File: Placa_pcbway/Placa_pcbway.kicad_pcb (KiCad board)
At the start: 2 copper layers, 100 x 100 mm, 69 parts, among them J1 Screw_Terminal_Crusher1, J2 MixerScrewTerminal1, J3 FanScrewTerminal1, K1 FINDER-36.11, K2 FINDER-36.11, K3 FINDER-36.11, Q1 2N3904, Q2 2N3904, Q3 2N3904, U1 LM7805_TO220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

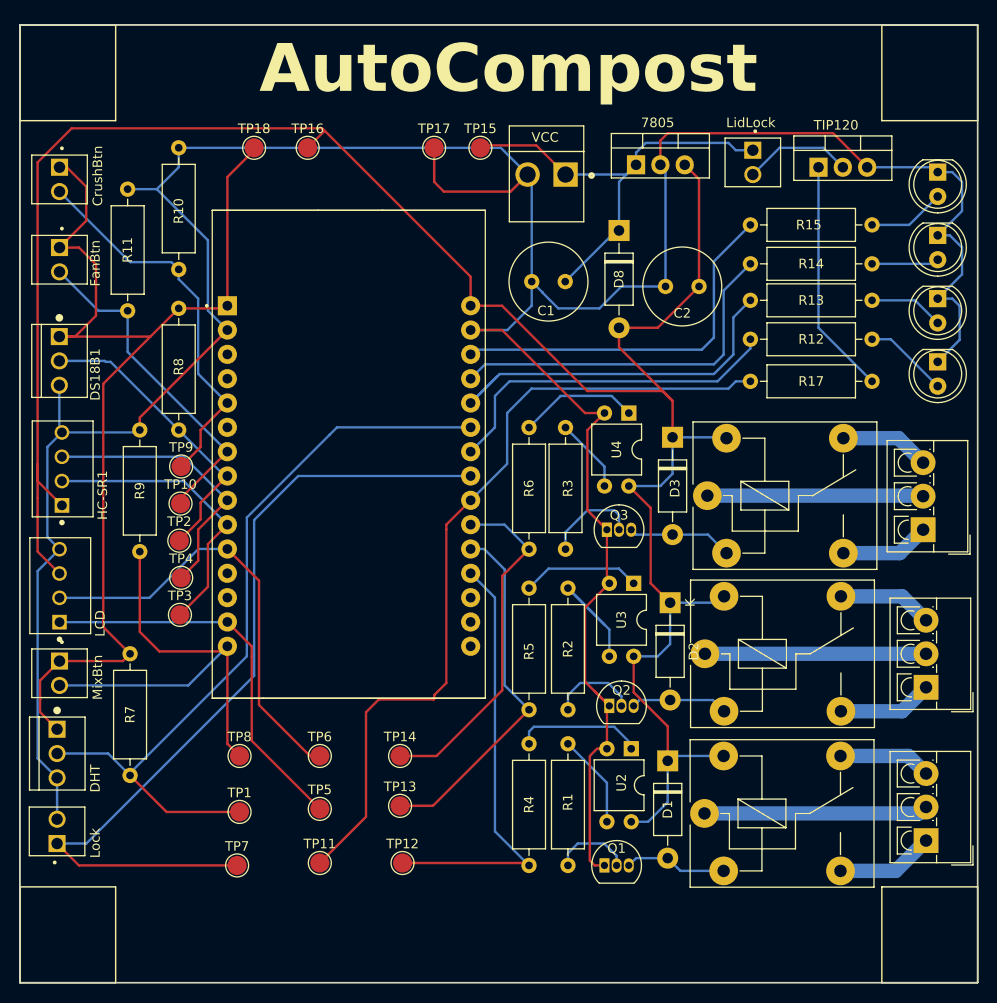
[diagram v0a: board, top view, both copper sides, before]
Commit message: Placa Pcbway terminada
Se agrandaron los agujeros correspondientes, se agregaron los agujeros de placa y el DRC pass
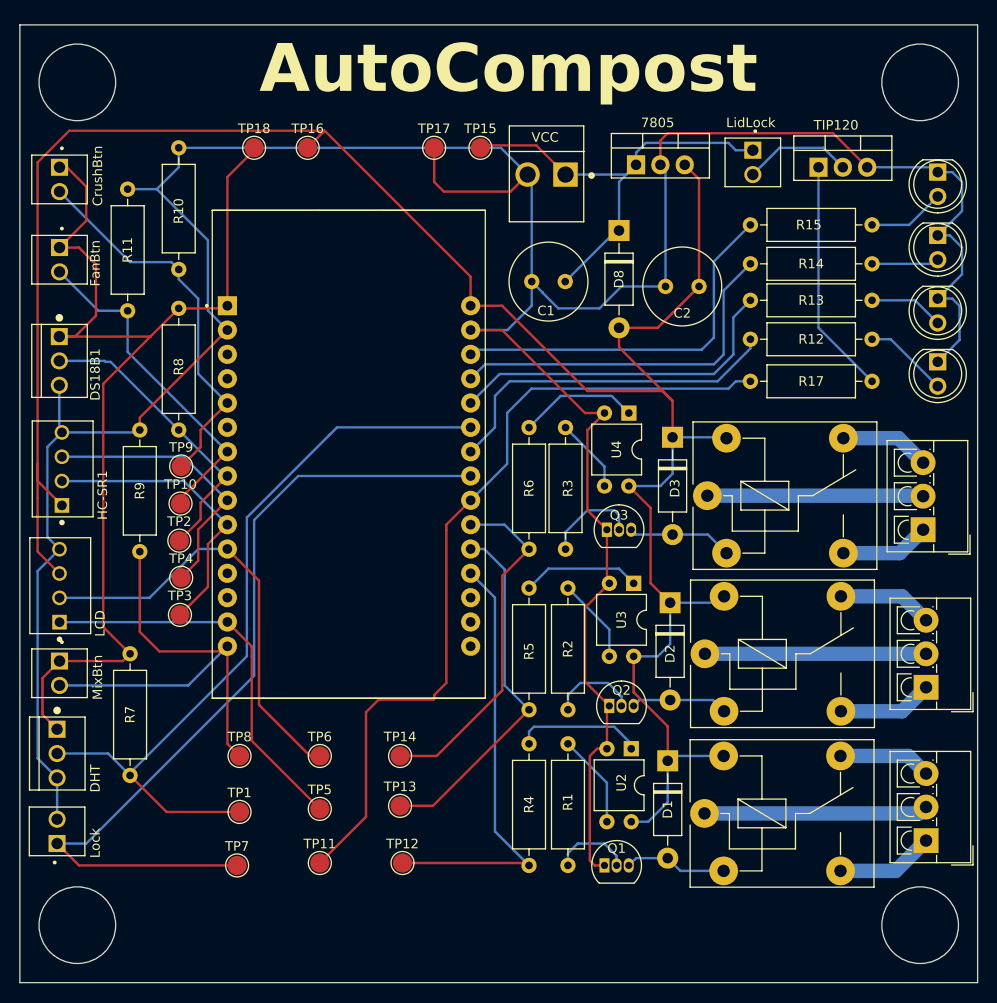
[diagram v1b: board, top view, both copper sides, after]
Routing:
- net Net-(R2-Pad1): track 14.3 -> 8.91 mm
- net /Led2: track 39.8 -> 35.9 mm
- net GND: track 334.6 -> 332.5 mm
- net /3V3: track 115.5 -> 115.0 mm
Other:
- outline, holes or cut-outs redrawn

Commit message: Placa pcbway terminada sin plano de tierra
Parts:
- removed D7: LED, LED_THT:LED_D5.0mm
- removed R15: 220, Resistor_THT:R_Axial_DIN0309_L9.0mm_D3.2mm_P12.70mm_Horizontal
- J1: value Screw_Terminal_Crusher1 -> Molex 0.156; footprint TerminalBlock_4Ucon:TerminalBlock_4Ucon_1x03_P3.50mm_Vertical -> Conectores_Molex:Molex_156_3pines
- J2: value MixerScrewTerminal1 -> Molex 0.156; footprint TerminalBlock_4Ucon:TerminalBlock_4Ucon_1x03_P3.50mm_Vertical -> Conectores_Molex:Molex_156_3pines
- J3: value FanScrewTerminal1 -> Molex 0.156; footprint TerminalBlock_4Ucon:TerminalBlock_4Ucon_1x03_P3.50mm_Vertical -> Conectores_Molex:Molex_156_3pines
- moved J2 3.53 mm to (195.1, 105.7), turned to -90 degrees
- moved J1 3.28 mm to (195.1, 121.9), turned to -90 degrees
- moved J3 3.14 mm to (195.1, 89.7), turned to -90 degrees
- moved K1 0.25 mm to (171.7, 122.3)
- moved K2 0.20 mm to (171.7, 105.7)
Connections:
- U5 pad 19: /Crusher -> /Lid
- U5 pad 20: /Mixer -> unconnected-(U5-D35-Pad20)
- U5 pad 22: /Lock -> /Crusher
- U5 pad 23: /Lid -> /Mixer
- U5 pad 24: /Led1 -> /Lock
- U5 pad 26: /Led2 -> /Led1
- U5 pad 27: /Led3 -> /Led2
- U5 pad 28: /Led4 -> /Led3
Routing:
- net /Led4: track 39.5 -> 0.00 mm
- net /Lid: track 88.3 -> 78.2 mm
- net Net-(D7-A): track 8.60 -> 0.00 mm
- net /Crusher: track 46.3 -> 54.0 mm
- net /Mixer: track 37.8 -> 44.5 mm
- net GND: track 332.5 -> 327.4 mm
- net /Led3: track 38.4 -> 33.8 mm
- net /Led1: track 36.6 -> 32.0 mm
- net /Led2: track 35.9 -> 33.4 mm
- net Net-(J3-Pad3): track 9.39 -> 10.1 mm
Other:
- outline, holes or cut-outs redrawn
- board text added: "CRUSHER"
- board text added: "FAN"
- board text added: "MIXER"

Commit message: Placa con plano de tierra
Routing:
- added copper zone on B.Cu, net GND
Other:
- outline, holes or cut-outs redrawn
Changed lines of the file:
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@@
   (gr_circle (center 106 46) (end 110 46)
+    (stroke (width 0.1) (type default)) (fill none) (layer "Edge.Cuts"))
+  (gr_rect (start 184.15 80.137) (end 197.866 80.899)
     (stroke (width 0.1) (type default)) (fill none) (layer "Edge.Cuts"))
   (gr_text "DS18B1" (at 108.458 79.248 90) (layer "F.SilkS")
@@
   (segment (start 194.302 85.702) (end 195.072 85.702) (width 1.5) (layer "B.Cu") (net 56))
   (segment (start 191.754 83.154) (end 194.302 85.702) (width 1.5) (layer "B.Cu") (net 56))
+  (zone (net 2) (net_name "GND") (layer "B.Cu") (hatch edge 0.5)
+    (connect_pads (clearance 0.5))
+    (min_thickness 0.25) (filled_areas_thickness no)
+    (fill yes (thermal_gap 0.5) (thermal_bridge_width 0.5))
+    (polygon
+      (pts
+        (xy 170.053 79.756)
+        (xy 199.517 79.756)
+        (xy 199.517 50.546)
+        (xy 100.965 50.419)
+        (xy 100.838 128.778)
+        (xy 169.926 128.905)
+        (xy 169.926 125.222)
+        (xy 168.402 123.698)
+        (xy 168.402 121.158)
+        (xy 169.926 119.507)
+        (xy 169.926 108.204)
+        (xy 168.656 107.061)
+        (xy 168.656 104.394)
+        (xy 169.926 102.997)
+        (xy 169.926 91.948)
+        (xy 168.656 90.678)
+        (xy 168.656 87.884)
+        (xy 170.053 86.233)
+      )
+    )
+  )
 )

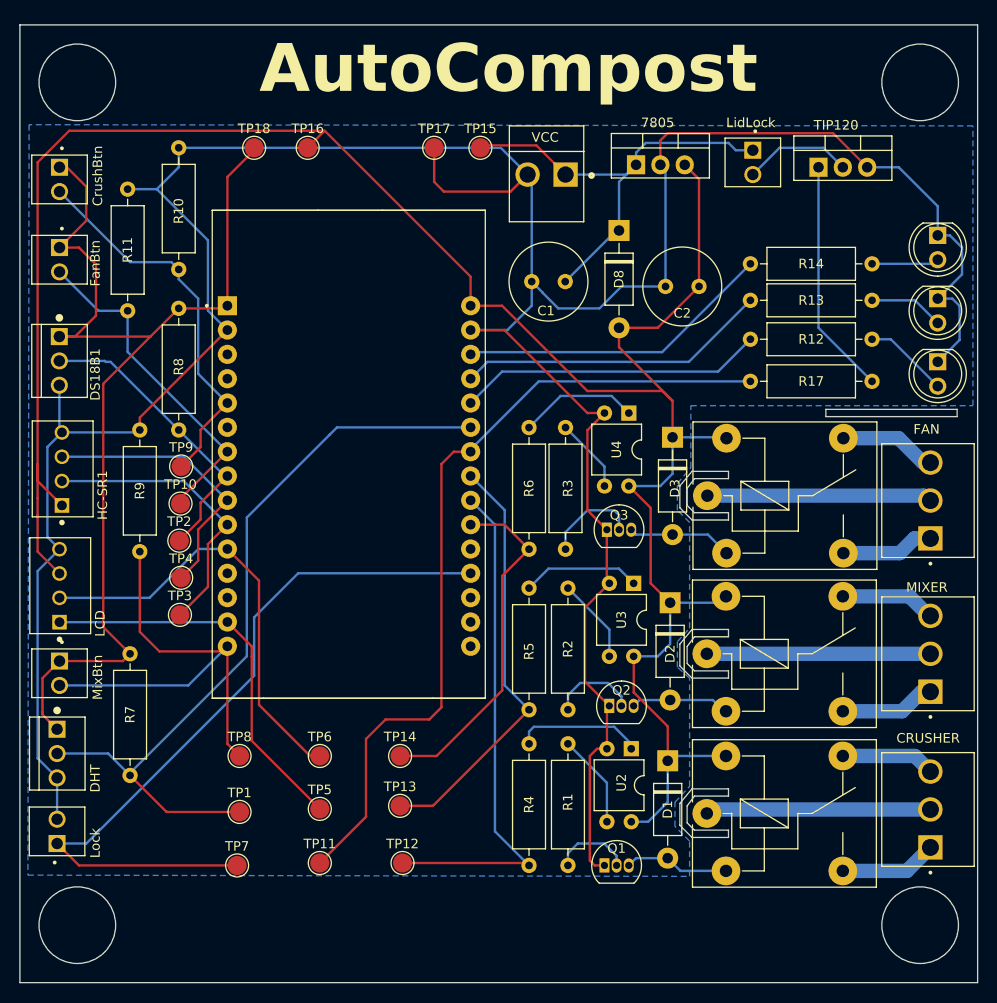
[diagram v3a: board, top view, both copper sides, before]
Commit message: Correccion Fan Button
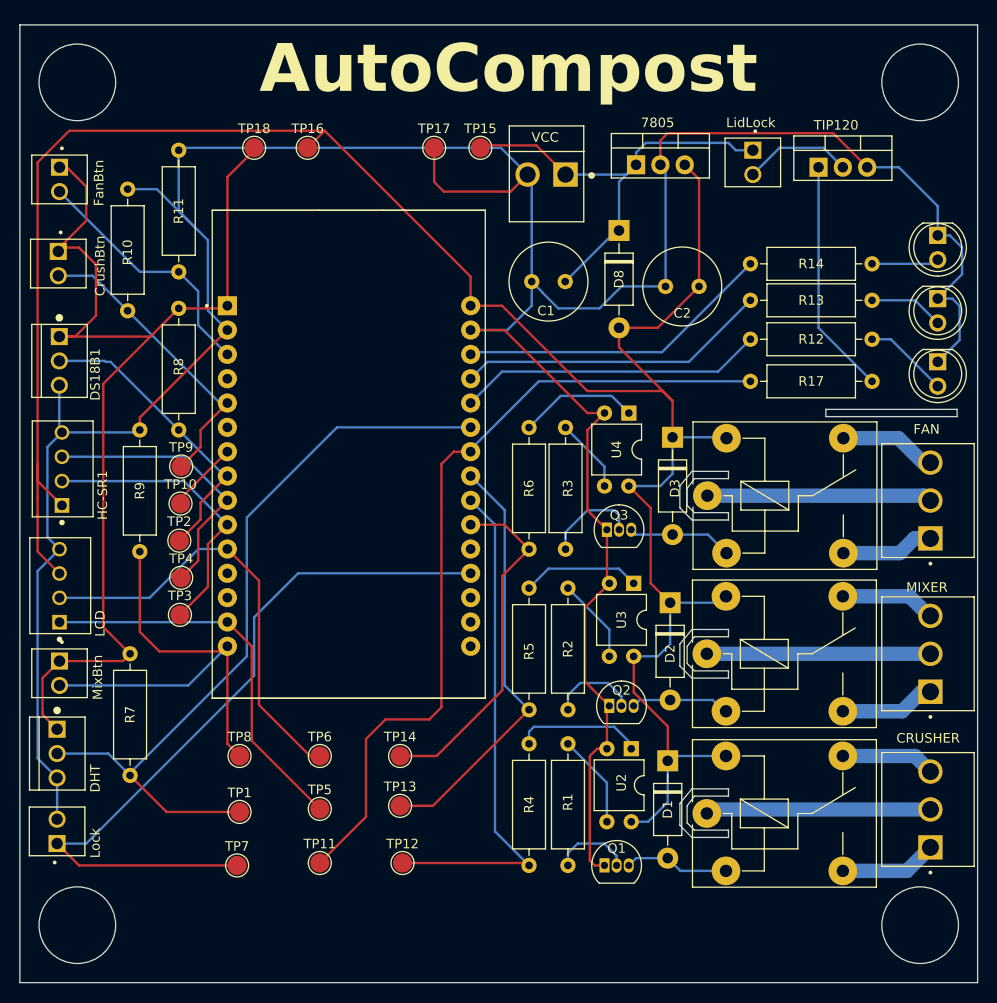
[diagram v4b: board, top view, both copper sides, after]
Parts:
- moved CrusherButton1 8.78 mm to (104.0, 64.9)
- moved FanButton1 8.38 mm to (104.1, 56.1)
- moved R10 6.86 mm to (111.3, 57.1)
- moved R11 6.71 mm to (116.6, 53.1)
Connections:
- U5 pad 3: unconnected-(U5-D15-Pad3) -> /FanBtn
- U5 pad 7: /FanBtn -> unconnected-(U5-TX2-Pad7)
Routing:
- net /CrusherBtn: track 40.5 -> 31.8 mm
- net GND: track 327.4 -> 332.8 mm
- net /FanBtn: track 35.3 -> 34.1 mm
- removed copper zone on B.Cu, net GND
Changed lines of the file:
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@@
   (net 44 "unconnected-(U5-VP-Pad17)")
   (net 45 "unconnected-(U5-EN-Pad16)")
-  (net 46 "unconnected-(U5-D15-Pad3)")
+  (net 46 "unconnected-(U5-TX2-Pad7)")
   (net 47 "unconnected-(U5-D35-Pad20)")
   (net 48 "Net-(J1-Pad1)")
@@
   )
   (footprint "Resistor_THT:R_Axial_DIN0309_L9.0mm_D3.2mm_P12.70mm_Horizontal" (layer "F.Cu")
-    (at 116.586 52.832 -90)
+    (at 111.252 57.15 -90)
     (descr "Resistor, Axial_DIN0309 series, Axial, Horizontal, pin pitch=12.7mm, 0.5W = 1/2W, length*diameter=9*3.2mm^2, http://cdn-reichelt.de/documents/datenblatt/B400/1_4W%23YAG.pdf")
     (tags "Resistor Axial_DIN0309 series Axial Horizontal pin pitch 12.7mm 0.5W = 1/2W length 9mm diameter 3.2mm")
@@
   )
   (footprint "Resistor_THT:R_Axial_DIN0309_L9.0mm_D3.2mm_P12.70mm_Horizontal" (layer "F.Cu")
-    (at 111.252 57.15 -90)
+    (at 116.586 53.086 -90)
     (descr "Resistor, Axial_DIN0309 series, Axial, Horizontal, pin pitch=12.7mm, 0.5W = 1/2W, length*diameter=9*3.2mm^2, http://cdn-reichelt.de/documents/datenblatt/B400/1_4W%23YAG.pdf")
     (tags "Resistor Axial_DIN0309 series Axial Horizontal pin pitch 12.7mm 0.5W = 1/2W length 9mm diameter 3.2mm")
@@
         (effects (font (size 1 1) (thickness 0.15)))
     )
-    (fp_text value "TestPoint" (at 0 2.05) (layer "F.Fab")
+    (fp_text value "TestPoint" (at 0 2.05) (layer "F.Fab") hide
         (effects (font (size 1 1) (thickness 0.15)))
     )
@@
         (effects (font (size 1 1) (thickness 0.15)))
     )
-    (fp_text value "TestPoint" (at 0 2.05) (layer "F.Fab")
+    (fp_text value "TestPoint" (at 0 2.05) (layer "F.Fab") hide
         (effects (font (size 1 1) (thickness 0.15)))
     )
@@
   )
   (footprint "Conectores_Molex:Molex_100_2pines" (layer "F.Cu")
-    (at 104.14 56.134 90)
+    (at 104.013 64.918 90)
     (property "Availability" "In Stock")
     (property "Check_prices" "https://www.snapeda.com/parts/0022272021/Molex/view-part/?ref=eda")
@@
       (net 2 "GND") (pinfunction "GND") (pintype "power_in") (solder_mask_margin 0.102))
     (pad "3" thru_hole circle (at -12.7 -10.435) (size 2 2) (drill 1.02) (layers "*.Cu" "*.Mask")
-      (net 46 "unconnected-(U5-D15-Pad3)") (pinfunction "D15") (pintype "bidirectional") (solder_mask_margin 0.102))
+      (net 14 "/FanBtn") (pinfunction "D15") (pintype "bidirectional") (solder_mask_margin 0.102))
     (pad "4" thru_hole circle (at -12.7 -7.895) (size 2 2) (drill 1.02) (layers "*.Cu" "*.Mask")
       (net 42 "unconnected-(U5-D2-Pad4)") (pinfunction "D2") (pintype "bidirectional") (solder_mask_margin 0.102))
@@
       (net 39 "unconnected-(U5-RX2-Pad6)") (pinfunction "RX2") (pintype "input") (solder_mask_margin 0.102))
     (pad "7" thru_hole circle (at -12.7 -0.275) (size 2 2) (drill 1.02) (layers "*.Cu" "*.Mask")
-      (net 14 "/FanBtn") (pinfunction "TX2") (pintype "output") (solder_mask_margin 0.102))
+      (net 46 "unconnected-(U5-TX2-Pad7)") (pinfunction "TX2") (pintype "output") (solder_mask_margin 0.102))
     (pad "8" thru_hole circle (at -12.7 2.265) (size 2 2) (drill 1.02) (layers "*.Cu" "*.Mask")
       (net 13 "/DS18B20") (pinfunction "D5") (pintype "bidirectional") (solder_mask_margin 0.102))
@@
   )
   (footprint "Conectores_Molex:Molex_100_2pines" (layer "F.Cu")
-    (at 104.14 64.516 90)
+    (at 104.14 56.134 90)
     (property "Availability" "In Stock")
     (property "Check_prices" "https://www.snapeda.com/parts/0022272021/Molex/view-part/?ref=eda")
@@
     (effects (font (size 1 1) (thickness 0.15)) (justify left bottom))
   )
-  (gr_text "CrushBtn" (at 108.712 58.928 90) (layer "F.SilkS")
+  (gr_text "CrushBtn" (at 108.966 68.326 90) (layer "F.SilkS")
     (effects (font (size 1 1) (thickness 0.15)) (justify left bottom))
   )
@@
     (effects (font (size 1 1) (thickness 0.15)) (justify left bottom))
   )
-  (gr_text "FanBtn" (at 108.458 67.31 90) (layer "F.SilkS")
+  (gr_text "FanBtn" (at 108.839 58.928 90) (layer "F.SilkS")
     (effects (font (size 1 1) (thickness 0.15)) (justify left bottom))
   )
@@
   (segment (start 161.29 98.049) (end 161.549 98.308) (width 0.25) (layer "F.Cu") (net 2))
   (segment (start 195.834 68.58) (end 197.358 68.58) (width 0.25) (layer "B.Cu") (net 2))
-  (segment (start 114.3 57.15) (end 116.586 54.864) (width 0.25) (layer "B.Cu") (net 2))
   (segment (start 167.414 55.146) (end 166.878 54.61) (width 0.25) (layer "B.Cu") (net 2))
   (segment (start 195.834 61.976) (end 197.104 61.976) (width 0.25) (layer "B.Cu") (net 2))
-  (segment (start 114.3 57.15) (end 119.634 62.484) (width 0.25) (layer "B.Cu") (net 2))
   (segment (start 104.12 82.276) (end 104.394 82.55) (width 0.25) (layer "B.Cu") (net 2))
   (segment (start 153.444 66.802) (end 154.587 67.945) (width 0.25) (layer "B.Cu") (net 2))
@@
   (segment (start 103.886 122.936) (end 103.886 118.618) (width 0.25) (layer "B.Cu") (net 2))
   (segment (start 197.358 68.58) (end 198.12 69.342) (width 0.25) (layer "B.Cu") (net 2))
+  (segment (start 116.586 53.086) (end 116.586 59.436) (width 0.25) (layer "B.Cu") (net 2))
   (segment (start 104.12 77.6235) (end 104.12 82.276) (width 0.25) (layer "B.Cu") (net 2))
   (segment (start 111.252 57.15) (end 114.3 57.15) (width 0.25) (layer "B.Cu") (net 2))
@@
   (segment (start 102.87 93.472) (end 104.14 94.742) (width 0.25) (layer "B.Cu") (net 2))
   (segment (start 198.374 63.246) (end 198.374 66.04) (width 0.25) (layer "B.Cu") (net 2))
+  (segment (start 116.586 59.436) (end 118.237 61.087) (width 0.25) (layer "B.Cu") (net 2))
+  (segment (start 118.237 61.087) (end 119.634 62.484) (width 0.25) (layer "B.Cu") (net 2))
   (segment (start 198.374 66.04) (end 195.834 68.58) (width 0.25) (layer "B.Cu") (net 2))
   (segment (start 153.444 69.314) (end 153.444 66.802) (width 0.25) (layer "B.Cu") (net 2))
+  (segment (start 114.3 57.15) (end 118.237 61.087) (width 0.25) (layer "B.Cu") (net 2))
   (segment (start 198.12 69.342) (end 198.12 72.893) (width 0.25) (layer "B.Cu") (net 2))
   (segment (start 147.066 71.861) (end 150.897 71.861) (width 0.25) (layer "B.Cu") (net 2))
@@
   (segment (start 118.872 82.296) (end 121.666 79.502) (width 0.25) (layer "F.Cu") (net 5))
   (segment (start 116.84 86.106) (end 118.872 84.074) (width 0.25) (layer "F.Cu") (net 5))
-  (segment (start 111.506 64.77) (end 115.824 64.77) (width 0.25) (layer "B.Cu") (net 5))
-  (segment (start 104.14 57.404) (end 111.506 64.77) (width 0.25) (layer "B.Cu") (net 5))
-  (segment (start 118.618 76.433) (end 121.666 79.481) (width 0.25) (layer "B.Cu") (net 5))
-  (segment (start 115.824 64.77) (end 116.586 65.532) (width 0.25) (layer "B.Cu") (net 5))
-  (segment (start 118.618 68.58) (end 118.618 76.433) (width 0.25) (layer "B.Cu") (net 5))
-  (segment (start 116.586 65.532) (end 116.586 66.548) (width 0.25) (layer "B.Cu") (net 5))
-  (segment (start 116.586 66.548) (end 118.618 68.58) (width 0.25) (layer "B.Cu") (net 5))
+  (segment (start 111.252 69.85) (end 120.883 79.481) (width 0.25) (layer "B.Cu") (net 5))
+  (segment (start 120.883 79.481) (end 121.666 79.481) (width 0.25) (layer "B.Cu") (net 5))
+  (segment (start 104.013 66.188) (end 107.59 66.188) (width 0.25) (layer "B.Cu") (net 5))
+  (segment (start 107.59 66.188) (end 111.252 69.85) (width 0.25) (layer "B.Cu") (net 5))
   (segment (start 167.64 127) (end 164.338 127) (width 0.25) (layer "B.Cu") (net 6))
   (segment (start 164.338 127) (end 163.576 127.762) (width 0.25) (layer "B.Cu") (net 6))
@@
   (segment (start 116.7765 89.4505) (end 116.7765 89.9795) (width 0.25) (layer "F.Cu") (net 14))
   (segment (start 121.666 84.561) (end 116.7765 89.4505) (width 0.25) (layer "F.Cu") (net 14))
-  (segment (start 111.252 74.147) (end 121.666 84.561) (width 0.25) (layer "B.Cu") (net 14))
-  (segment (start 111.252 69.85) (end 111.252 74.147) (width 0.25) (layer "B.Cu") (net 14))
-  (segment (start 108.204 69.85) (end 111.252 69.85) (width 0.25) (layer "B.Cu") (net 14))
-  (segment (start 104.14 65.786) (end 108.204 69.85) (width 0.25) (layer "B.Cu") (net 14))
+  (segment (start 112.522 65.786) (end 104.14 57.404) (width 0.25) (layer "B.Cu") (net 14))
+  (segment (start 118.618 67.818) (end 118.618 71.353) (width 0.25) (layer "B.Cu") (net 14))
+  (segment (start 118.618 71.353) (end 121.666 74.401) (width 0.25) (layer "B.Cu") (net 14))
+  (segment (start 116.586 65.786) (end 118.618 67.818) (width 0.25) (layer "B.Cu") (net 14))
+  (segment (start 116.586 65.786) (end 112.522 65.786) (width 0.25) (layer "B.Cu") (net 14))
   (segment (start 121.666 92.181) (end 119.634 94.213) (width 0.25) (layer "F.Cu") (net 15))
   (segment (start 119.634 98.679) (end 116.713 101.6) (width 0.25) (layer "F.Cu") (net 15))
@@
   (segment (start 194.302 85.702) (end 195.072 85.702) (width 1.5) (layer "B.Cu") (net 56))
   (segment (start 191.754 83.154) (end 194.302 85.702) (width 1.5) (layer "B.Cu") (net 56))
-  (zone (net 2) (net_name "GND") (layer "B.Cu") (hatch edge 0.5)
-    (connect_pads (clearance 0.5))
-    (min_thickness 0.25) (filled_areas_thickness no)
-    (fill yes (thermal_gap 0.5) (thermal_bridge_width 0.5))
-    (polygon
-      (pts
-        (xy 170.053 79.756)
-        (xy 199.517 79.756)
-        (xy 199.517 50.546)
-        (xy 100.965 50.419)
-        (xy 100.838 128.778)
-        (xy 169.926 128.905)
-        (xy 169.926 125.222)
-        (xy 168.402 123.698)
-        (xy 168.402 121.158)
-        (xy 169.926 119.507)
-        (xy 169.926 108.204)
-        (xy 168.656 107.061)
-        (xy 168.656 104.394)
-        (xy 169.926 102.997)
-        (xy 169.926 91.948)
-        (xy 168.656 90.678)
-        (xy 168.656 87.884)
-        (xy 170.053 86.233)
-      )
-    )
-  )
 )
